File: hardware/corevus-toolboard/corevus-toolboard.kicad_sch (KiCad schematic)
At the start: 89 parts, among them J1 MF3, J10 1x3P, J2 XH, J3 MF3, J4 XH, J5 XH, J6 XH, J7 XH, J8 pinheader, J9 XH, Q2 NMOS, Q3 AO3401A, Q4 AO3400, Q5 AO3400, SW3 RST, U1 LIS2DE12, U2 TPS54302, U3 STM32G431KBU3, U4 TMC2209-LA, U5 74LVC1G17, U6 SPX3819M5-L-3-3, Y1 XRCGB25

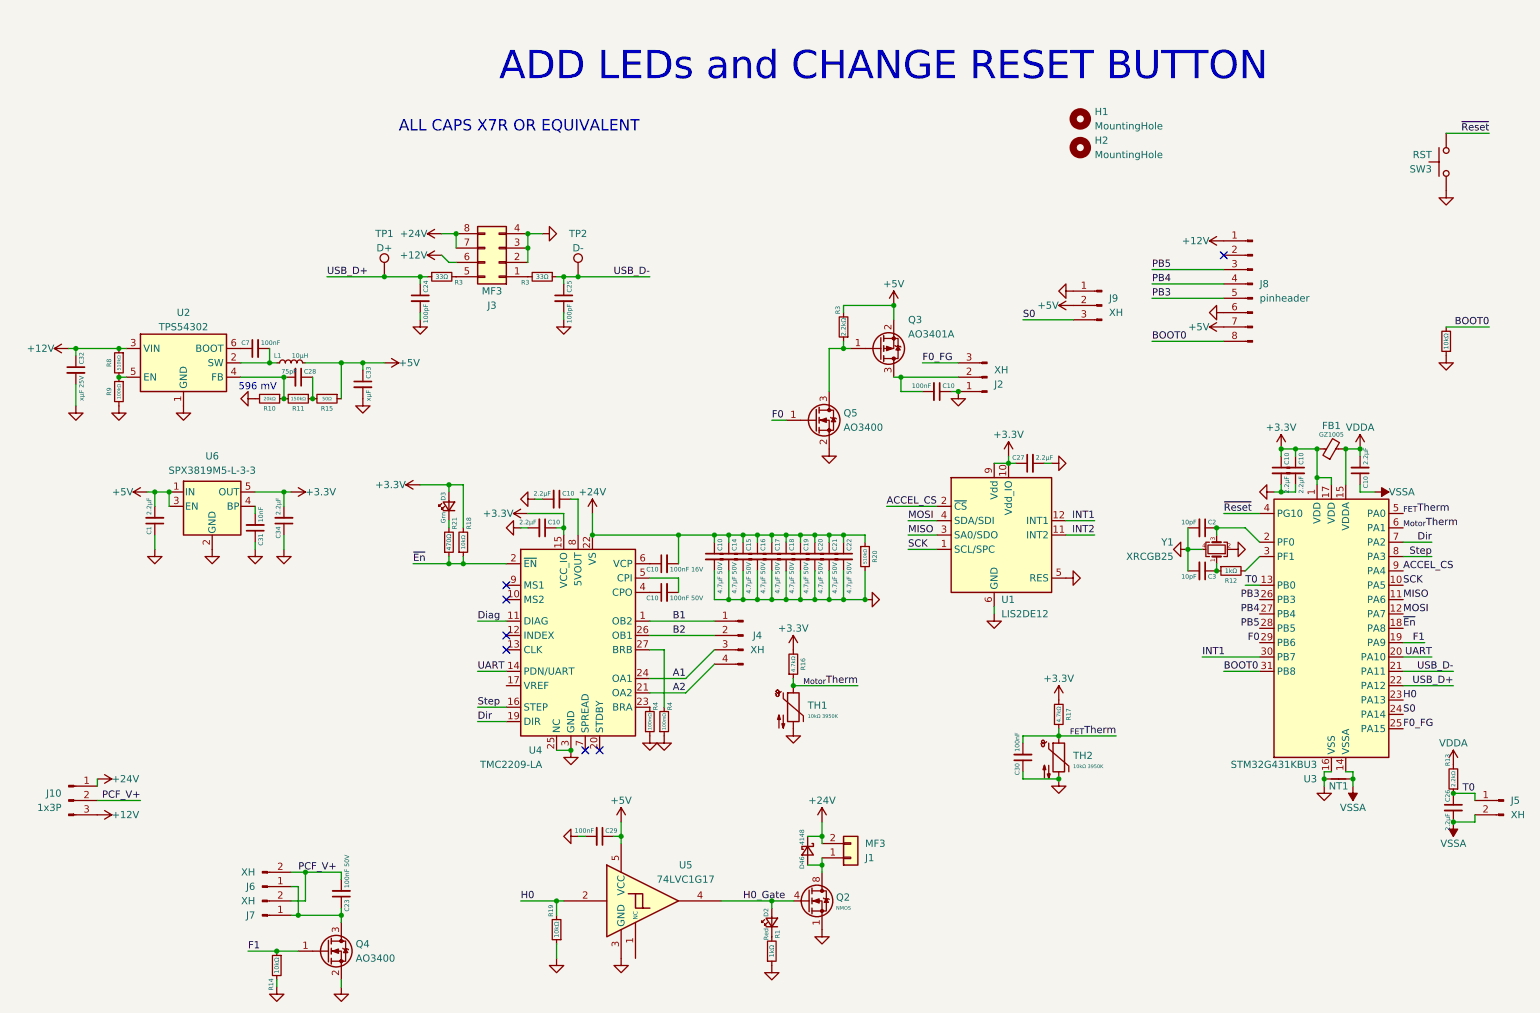
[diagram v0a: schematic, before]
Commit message: v0.3 toolboard nearing completion (just need to make the production files), also made panelization test board
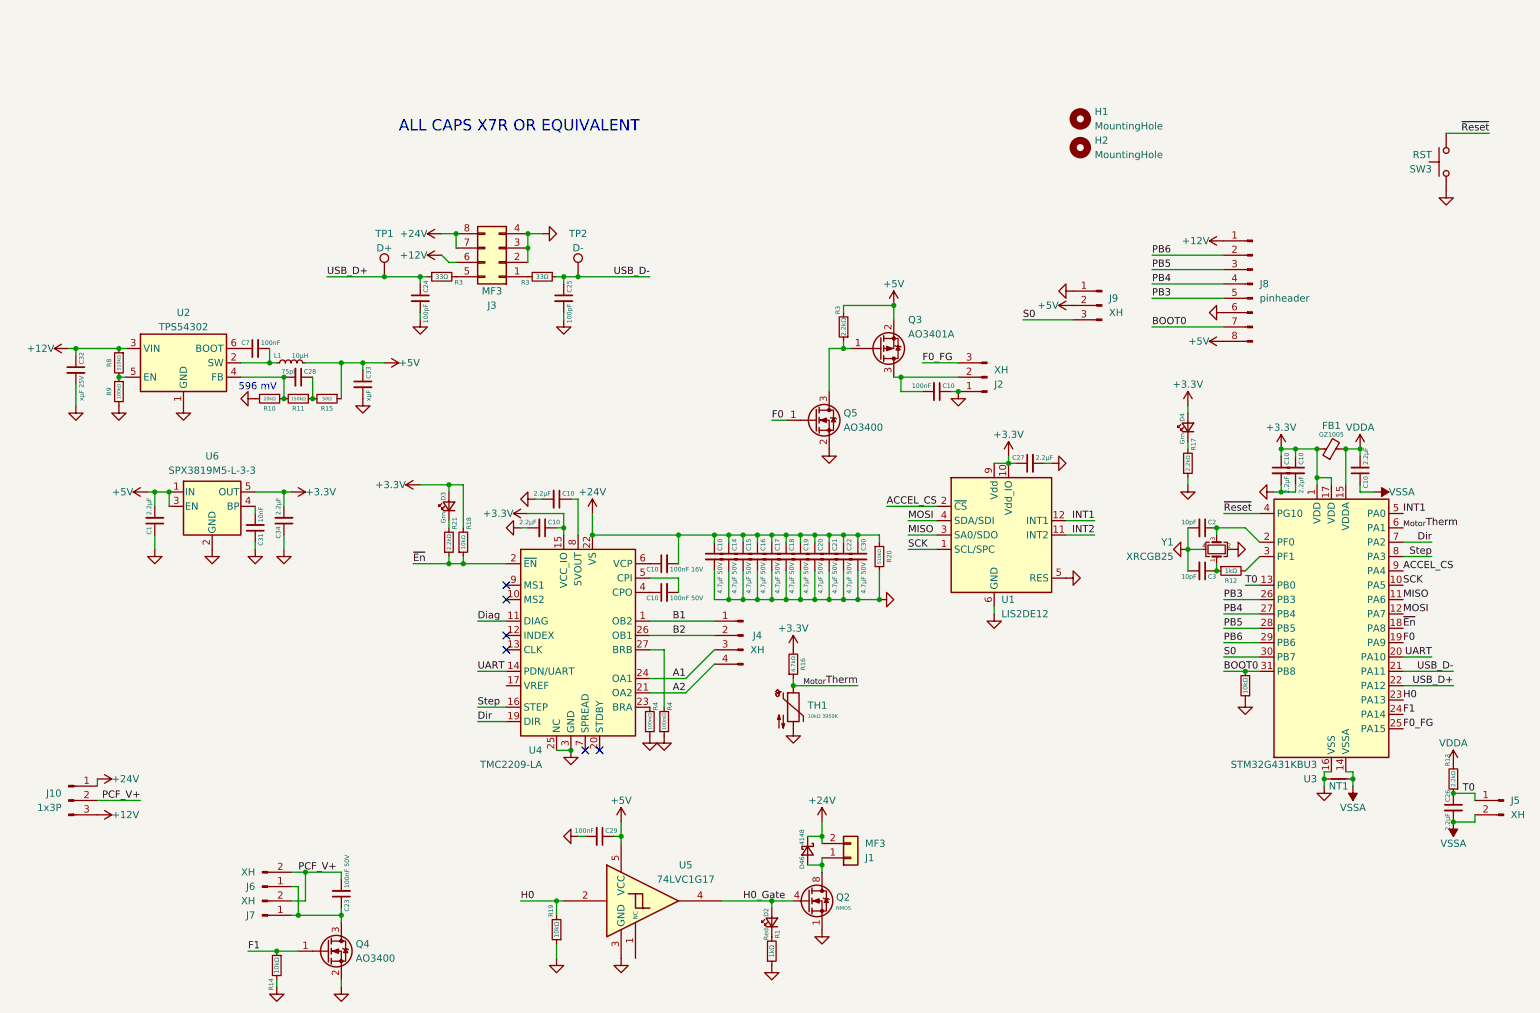
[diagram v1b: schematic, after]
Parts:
- removed TH2: 10kΩ 3950K, AlphaLib:0402R, symbol Device:Thermistor_NTC
- added D4: Grn, AlphaLib:0402LED, symbol Device:LED_Small
- C30: value 100nF -> 4.7µF 50V; footprint AlphaLib:0402C -> Capacitor_SMD:C_0805_2012Metric
- R17: value 4.7kΩ -> 2.2kΩ
- R21: value 470Ω -> 2.2kΩ
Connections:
- net +24V: now also C30.1
- net +3.3V: now also D4.2 (A); no longer R17.2
- net +5V: now also J8.8 (Pin_8); no longer J8.7 (Pin_7)
- net BOOT0: now also J8.7 (Pin_7); no longer J8.8 (Pin_8)
- net F0: now also U3.19 (PA9); no longer U3.29 (PB6)
- net F1: now also U3.24 (PA14); no longer U3.19 (PA9)
- net GND: now also C30.2, R17.1; no longer C30.1
- net INT1: now also U3.5 (PA0); no longer U3.30 (PB7)
- net S0: now also U3.30 (PB7); no longer U3.24 (PA14)
- net PB6: now reaches J8.2 (Pin_2)
- net PB6: now also U3.29 (PB6)
- removed net _{FET}Therm: C30.2, R17.1, U3.5 (PA0)
- new net: D4.1 (K), R17.2
- no-connect marks 7 -> 6
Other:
- note removed: "ADD LEDs and CHANGE RESET BUTTON"
- moved on the sheet: R20

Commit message: finished production data for toolboard v0.3, just waiting on parts eeeeeeee
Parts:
- C10: LCSC C1525 -> (none)
- C10: value 100nF 50V -> 22nF 50V; LCSC C1532 -> (none)
- C24, C25: value 100pF -> 10pF; LCSC C1525 -> (none)
- C28: value 75pF -> 68pF; LCSC C1525 -> (none)
- C32: value xµF 25V -> 10µF 25V
- C33: value xµF -> 10µF
- R15: value 50Ω -> 51Ω
- R4: LCSC C382279 -> (none)
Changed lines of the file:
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@@
 	(wire
 		(pts
+			(xy 77.47 85.09) (xy 77.47 83.82)
+		)
+		(stroke
+			(width 0)
+			(type default)
+		)
+	)
+	(wire
+		(pts
 			(xy 97.79 132.08) (xy 102.87 132.08)
 		)
@@
 			)
 		)
-		(property "LCSC" "C1525"
-			(at 130.81 113.03 90)
-			(effects
-				(font
-					(size 1.27 1.27)
-				)
-				(hide yes)
-			)
-		)
 		(pin "1"
 		)
@@
 			)
 		)
-		(property "Value" "100pF"
+		(property "Value" "10pF"
 			(at 88.63 67.04 90)
 			(effects
@@
 			)
 		)
-		(property "LCSC" "C1525"
-			(at 87.63 66.04 90)
-			(effects
-				(font
-					(size 1.27 1.27)
-				)
-				(hide yes)
-			)
-		)
 		(pin "1"
 		)
@@
 			)
 		)
-		(property "Value" "100nF 50V"
+		(property "Value" "22nF 50V"
 			(at 131.81 119.11 90)
 			(effects
@@
 			)
 		)
-		(property "LCSC" "C1532"
-			(at 130.81 118.11 90)
-			(effects
-				(font
-					(size 1.27 1.27)
-				)
-				(hide yes)
-			)
-		)
 		(pin "1"
 		)
@@
 			)
 		)
-		(property "LCSC" "C382279"
-			(at 128.27 140.97 90)
-			(effects
-				(font
-					(size 1.27 1.27)
-				)
-				(hide yes)
-			)
-		)
 		(pin "1"
 		)
@@
 			)
 		)
-		(property "LCSC" "C382279"
-			(at 130.81 140.97 90)
-			(effects
-				(font
-					(size 1.27 1.27)
-				)
-				(hide yes)
-			)
-		)
 		(pin "1"
 		)
@@
 			)
 		)
-		(property "Value" "xµF 25V"
+		(property "Value" "10µF 25V"
 			(at 27.67 79.74 90)
 			(effects
@@
 			)
 		)
-		(property "Value" "75pF "
+		(property "Value" "68pF "
 			(at 65.77 79.01 90)
 			(effects
@@
 			)
 		)
-		(property "LCSC" "C1525"
-			(at 66.04 80.01 90)
-			(effects
-				(font
-					(size 1.27 1.27)
-				)
-				(hide yes)
-			)
-		)
 		(pin "1"
 		)
@@
 			)
 		)
-		(property "Value" "50Ω"
+		(property "Value" "51Ω"
 			(at 71.12 83.82 90)
 			(effects
@@
 			)
 		)
-		(property "Value" "xµF"
+		(property "Value" "10µF"
 			(at 78.47 82.28 90)
 			(effects
@@
 			)
 		)
-		(property "Value" "100pF"
+		(property "Value" "10pF"
 			(at 114.03 67.04 90)
 			(effects
@@
 			)
 		)
-		(property "LCSC" "C1525"
-			(at 113.03 66.04 90)
-			(effects
-				(font
-					(size 1.27 1.27)
-				)
-				(hide yes)
-			)
-		)
 		(pin "1"
 		)
@@
 	(symbol
 		(lib_id "power:GND")
-		(at 77.47 83.82 0)
+		(at 77.47 85.09 0)
 		(unit 1)
 		(exclude_from_sim no)
@@
 		(dnp no)
 		(property "Reference" "#PWR056"
-			(at 77.47 90.17 0)
+			(at 77.47 91.44 0)
 			(effects
 				(font
@@
 		)
 		(property "Value" "GND"
-			(at 77.47 86.36 90)
+			(at 77.47 87.63 90)
 			(effects
 				(font
@@
 		)
 		(property "Footprint" ""
-			(at 77.47 83.82 0)
+			(at 77.47 85.09 0)
 			(effects
 				(font
@@
 		)
 		(property "Datasheet" ""
-			(at 77.47 83.82 0)
+			(at 77.47 85.09 0)
 			(effects
 				(font
@@
 		)
 		(property "Description" ""
-			(at 77.47 83.82 0)
+			(at 77.47 85.09 0)
 			(effects
 				(font

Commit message: should be up to date for cvg v0.6 and latest protected drivers
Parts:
- removed TP1: D+, symbol Connector:TestPoint
- removed TP2: D-, symbol Connector:TestPoint
- removed U5: 74LVC1G17, Package_TO_SOT_SMD:SOT-23-5, symbol 74xGxx:74LVC1G17
- added U5: MCP1416, Package_TO_SOT_SMD:SOT-23-5, symbol Driver_FET:MCP1416
- C10, C26, C27: value 2.2µF -> 1µF
- C24, C25: now not fitted; now left out of the parts list
- C29: value 100nF -> 1µF 25V
- R1: value 1kΩ -> 4.7kΩ
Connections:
- net +12V: now also C29.1, U5.2 (Vdd)
- net +5V: no longer C29.1
- net ACCEL_CS: now also U3.25 (PA15); no longer U3.9 (PA4)
- net Dir: now also U3.6 (PA1); no longer U3.7 (PA2)
- net F0_FG: no longer U3.25 (PA15)
- net GND: now also U5.1 (NC), U5.4 (GND)
- net H0: now also D2.2 (A), U5.3 (IN)
- net H0_Gate: now also U5.5 (OUT); no longer D2.2 (A)
- net INT1: now also U3.20 (PA10); no longer U1.12 (INT1), U3.5 (PA0)
- net PB6: no longer J8.2 (Pin_2), U3.29 (PB6)
- net T0: now also J5.2 (Pin_2); no longer J5.1 (Pin_1)
- net UART: now also U3.5 (PA0); no longer U3.20 (PA10)
- net VSSA: now also J5.1 (Pin_1); no longer J5.2 (Pin_2)
- net _{Motor}Therm: now also U3.7 (PA2); no longer U3.6 (PA1)
- net D+: now reaches J3.5 (Pin_5), R3.2
- net D-: now reaches J3.1 (Pin_1), R3.2
- net INT2: no longer names the net of U1.11 (INT2)
- net MISO renamed PA6
- net PA6: now also J8.4 (Pin_4); no longer U1.3 (SA0/SDO)
- net MOSI renamed PA7
- net PA7: now also J8.5 (Pin_5); no longer U1.4 (SDA/SDI)
- net PB3 renamed SPI1_SCK
- net SPI1_SCK: now also U1.1 (SCL/SPC); no longer J8.5 (Pin_5)
- net PB4 renamed SPI1_MISO
- net SPI1_MISO: now also U1.3 (SA0/SDO); no longer J8.4 (Pin_4)
- net PB5 renamed PA5
- net PA5: now also U3.10 (PA5); no longer U3.28 (PB5)
- removed net SCK: U1.1 (SCL/SPC), U3.10 (PA5)
- net USB_D+ renamed D+'
- net USB_D- renamed D-'
- new net PA4: J8.2 (Pin_2), U3.9 (PA4)
- new net SPI1_MOSI: U1.4 (SDA/SDI), U3.28 (PB5)
- no-connect marks 6 -> 8
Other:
- note added: "TODO: SOLDER JUMPER"
- moved on the sheet: C1, C10, C14, C15, C16, C17, C18, C19, C20, C21, C22, C29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

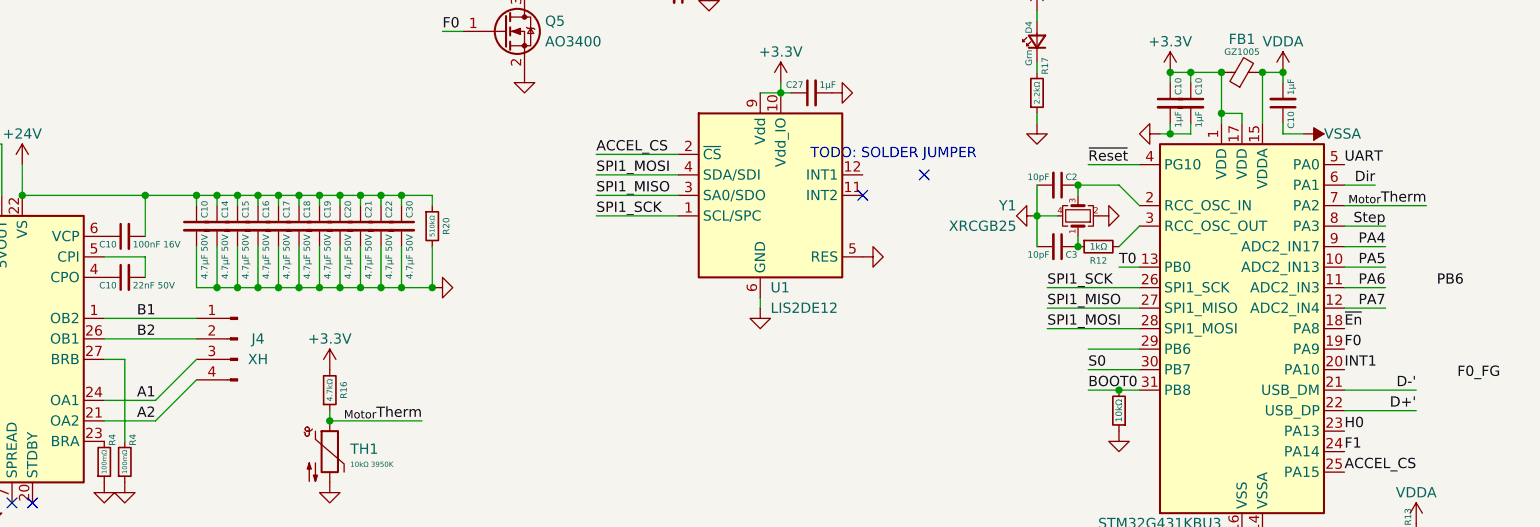
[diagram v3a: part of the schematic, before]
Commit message: Added details on fan / motor voltage selection
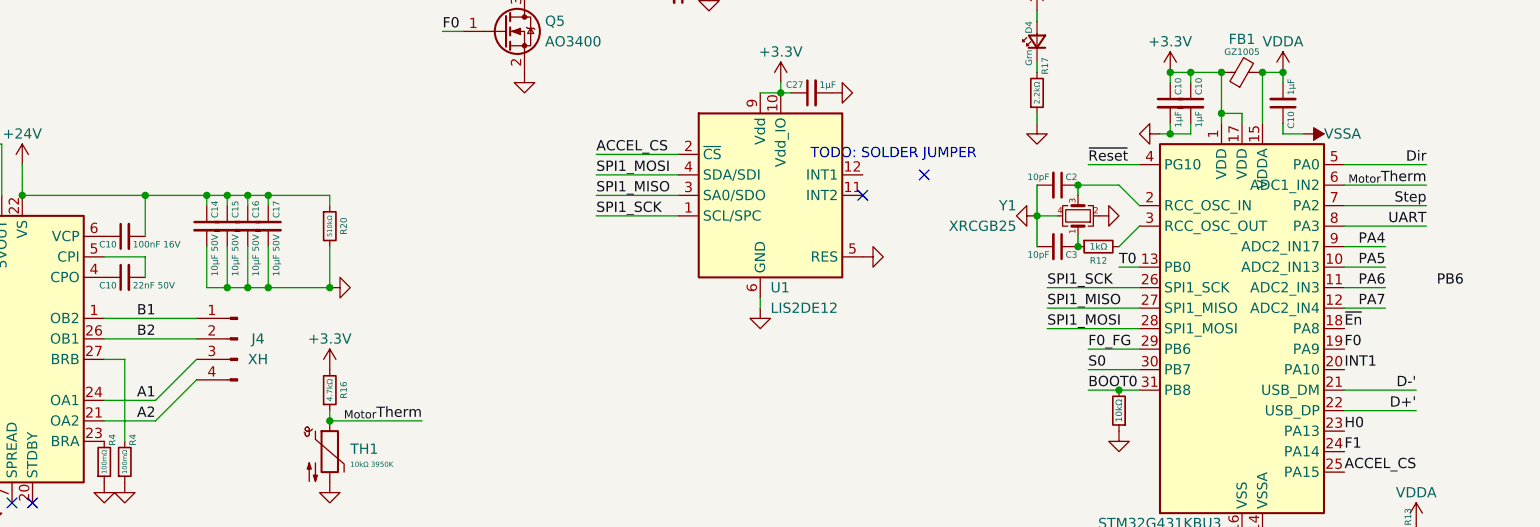
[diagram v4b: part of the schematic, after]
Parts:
- removed C10, C18, C19, C20, C21, C22, C30: 4.7µF 50V, Capacitor_SMD:C_0805_2012Metric, symbol Device:C_Small
- C14, C15, C16, C17: value 4.7µF 50V -> 10µF 50V; footprint Capacitor_SMD:C_0805_2012Metric -> Capacitor_SMD:C_1206_3216Metric
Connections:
- net Dir: now also U3.5 (PA0); no longer U3.6 (PA1)
- net F0_FG: now also U3.29 (PB6)
- net Step: now also U3.7 (PA2); no longer U3.8 (PA3)
- net UART: now also U3.8 (PA3); no longer U3.5 (PA0)
- net _{Motor}Therm: now also U3.6 (PA1); no longer U3.7 (PA2)
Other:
- moved on the sheet: C14, C15, C16, C17, R20
